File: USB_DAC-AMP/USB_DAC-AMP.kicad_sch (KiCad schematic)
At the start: 121 parts, among them J1 USB_C_Receptacle, J2 SJ-3524-SMT, SW1 SW_Push, U1 PCM2906, U10 NE5532, U11 NE5532, U2 TPS61040DBV, U3 SPX3819M5-L, U4 SPX3819M5-L, U5 NE5532, U6 NE5532, U7 NE5532, U8 NE5532, U9 NE5532, Y3 12 MHz Crystal

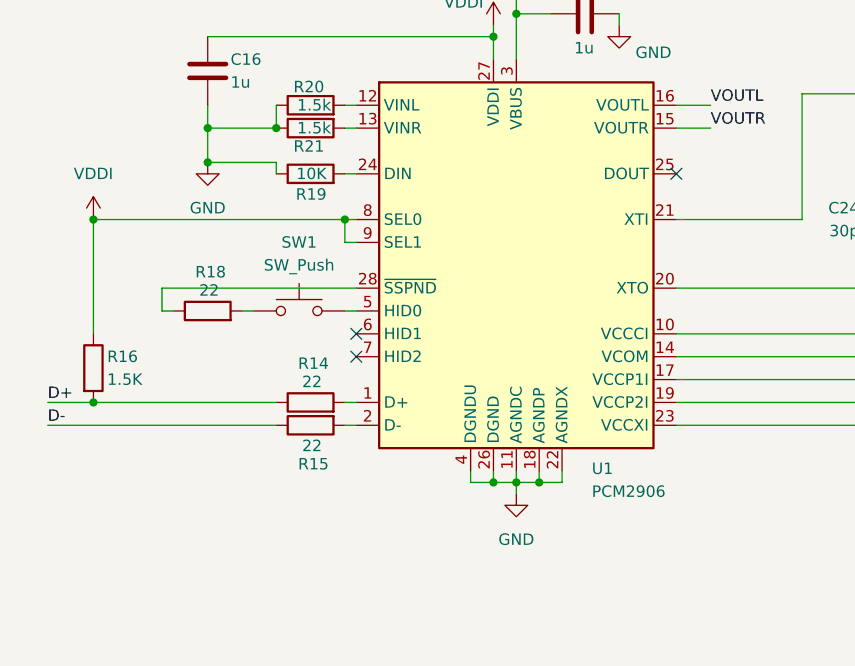
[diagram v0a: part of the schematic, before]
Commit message: finished V1 footprint assignments
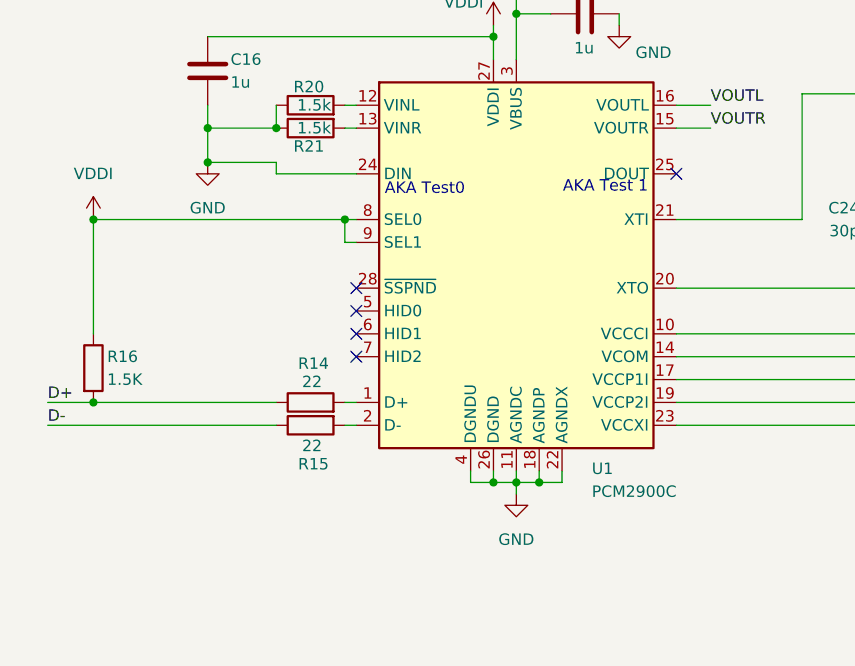
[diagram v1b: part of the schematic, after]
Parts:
- removed R18: 22, symbol Device:R
- removed R19: 10K, symbol Device:R
- removed SW1: SW_Push, symbol Switch:SW_Push
- C1, C10, C11, C12, C13, C16, C17, C18, C19, C2, C20, C21, C22, C23, C24, C26, C28, C29, C3, C32, C33, C34, C36, C38, C39, C4, C42, C43, C44, C46, C5, C6, C7, C8, C9: footprint (none) -> Capacitor_SMD:C_0603_1608Metric_Pad1.08x0.95mm_HandSolder
- C14, C15, C27, C30, C31, C35, C40, C41, C45: footprint (none) -> Capacitor_Tantalum_SMD:CP_EIA-7343-43_Kemet-X_HandSolder
- C25: footprint Capacitor_Tantalum_SMD:CP_EIA-7343-15_Kemet-W -> Capacitor_Tantalum_SMD:CP_EIA-7343-43_Kemet-X_HandSolder
- D1, D2, D6, D7: footprint (none) -> Diode_SMD:D_0603_1608Metric_Pad1.05x0.95mm_HandSolder
- D3: footprint (none) -> LED_SMD:LED_0603_1608Metric_Pad1.05x0.95mm_HandSolder
- F1: footprint (none) -> Fuse:Fuse_0603_1608Metric_Pad1.05x0.95mm_HandSolder
- FB1, FB2, FB3, FB4, FB5, R1, R10, R11, R12, R13, R14, R15, R16, R17, R2, R20, R21, R22, R23, R24, R25, R26, R27, R28, R29, R30, R31, R32, R33, R34, R35, R36, R38, R39, R40, R41, R42, R43, R5, R6, R7, R8, R9: footprint (none) -> Resistor_SMD:R_0603_1608Metric_Pad0.98x0.95mm_HandSolder
- J1: footprint (none) -> Connector_USB:USB_C_Receptacle_GCT_USB4105-xx-A_16P_TopMnt_Horizontal
- J2: footprint SJ-3524-SMT:CUI_SJ-3524-SMT -> Imported_footprints:SJ-3524-SMT
- L1: footprint (none) -> Inductor_SMD:L_0805_2012Metric_Pad1.05x1.20mm_HandSolder
- TP1, TP2, TP3, TP4, TP5: footprint (none) -> TestPoint:TestPoint_Pad_1.0x1.0mm
- U1: value PCM2906 -> PCM2900C
- U10, U11, U5, U6, U7, U8, U9: footprint (none) -> Package_SO:SOIC-8_5.3x5.3mm_P1.27mm
- Y3: footprint (none) -> Crystal:Crystal_SMD_3225-4Pin_3.2x2.5mm
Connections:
- net GND: now also U1.24 (DIN)
- no-connect marks 15 -> 17
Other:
- note added: "AKA Test 1"
- note added: "AKA Test0"
